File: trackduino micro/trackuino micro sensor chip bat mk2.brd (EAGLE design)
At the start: 50.4 x 19.5 mm, 39 parts, among them IC2 74AHC1G125DBV, U1 ATMEGA328P, Y1 16MHZ

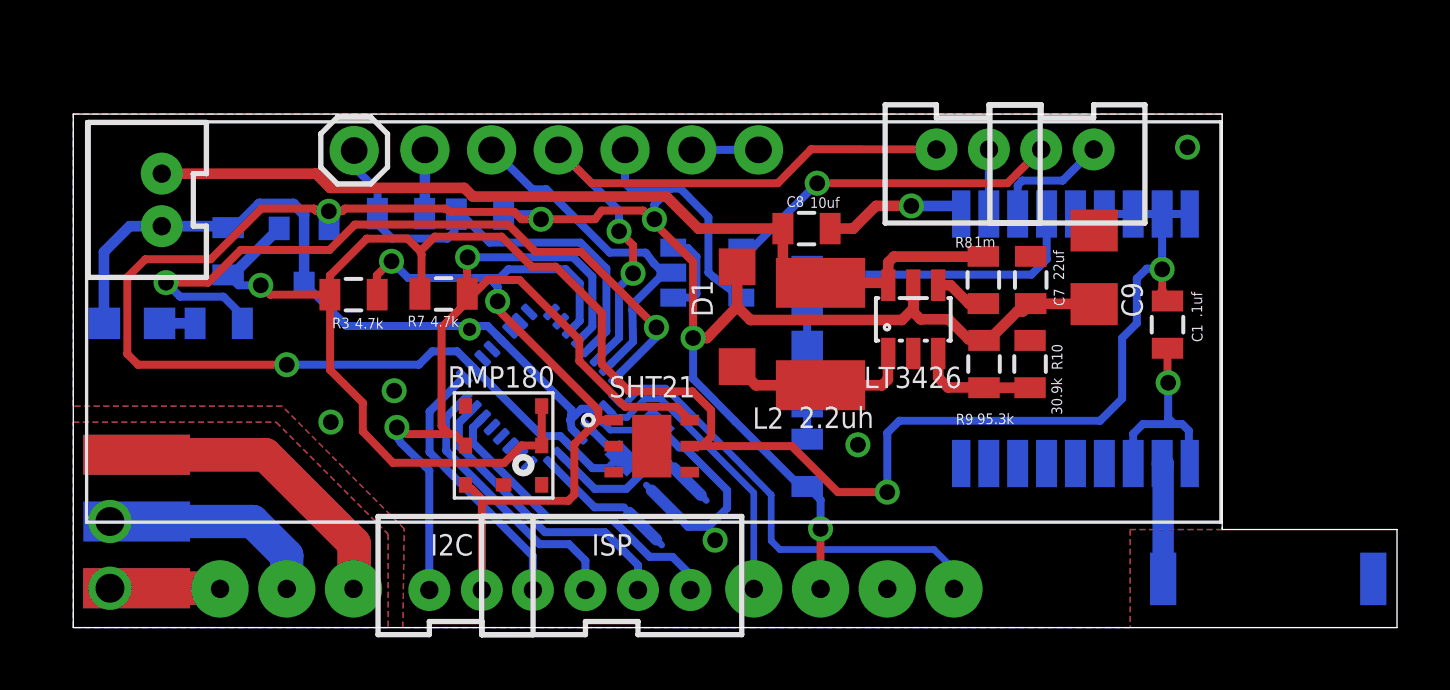
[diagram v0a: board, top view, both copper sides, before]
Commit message: SilkScreen Clean Up and Battery
Cleaned up silk screen and created a board revision with a GPS backup
battery
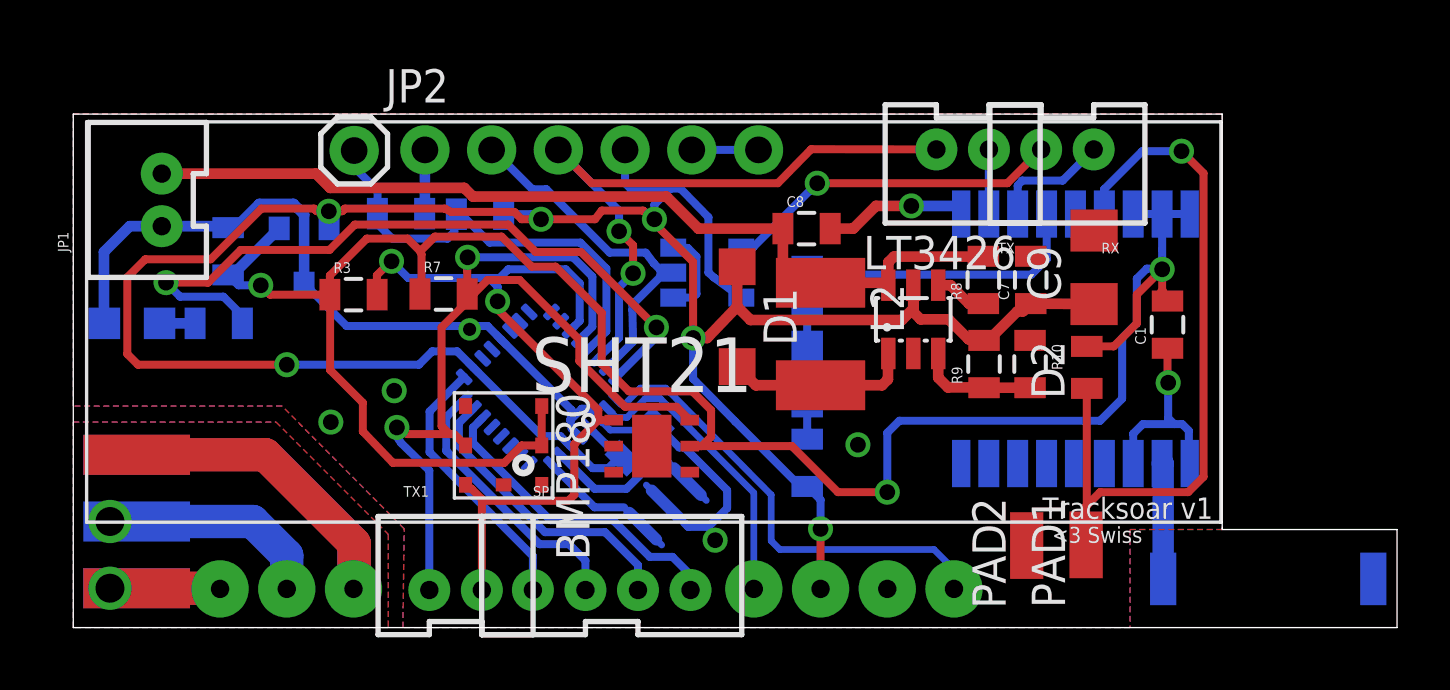
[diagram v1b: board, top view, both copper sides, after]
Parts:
- added D2: (no value), diode:MICROMELF-R
- added PAD1, PAD2: WIREPADSMD1,27-254, wirepad:SMD1,27-2,54
- U1: value ATMEGA328P -> ATMEGA168MLF
- renumbered GPS-ANT to U$3
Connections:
- new net N$2: D2.C, PAD1.1, U$1.6_V_BCKP
- net 3V: now also D2.A; no longer U$1.6_V_BCKP
- net GND: now also PAD2.1
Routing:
- net N$2: track 0.00 -> 28.1 mm, vias 0 -> 1
- net 3V: track 78.0 -> 81.7 mm
- net GND: vias 9 -> 8
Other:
- board text removed: "+"
- board text removed: "-"
- board text removed: "FTDI"
- board text removed: "GND"
- board text removed: "I2C"
- board text removed: "ISP"
